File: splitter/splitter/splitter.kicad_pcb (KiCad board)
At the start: 2 copper layers, 50.8 x 89.4 mm, 35 parts, among them J1 JACKIN, J10 Conn_01x08, J11 Conn_01x08, J2 JACKSEND, J3 JACKRECV, J4 JACKOUT, J5 Jack-DC, J6 JACKSEND2, J7 RING_SEND, J8 JACKRECV2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

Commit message: more adjustments
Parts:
- moved U2 5.08 mm to (22.0, 21.8), turned to 90 degrees
- moved C3 5.01 mm to (23.4, 25.6), turned to -90 degrees
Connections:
- D1 pad 2: +9V -> /LED
- J10 pad 1: /DC_IN -> +9V
- J10 pad 2: +9V -> /LED
- J11 pad 1: /DC_IN_B -> /9V_B
- J11 pad 2: /9V_B -> /LED_B
- J5 pad 1: /DC_IN -> +9V
- SW2 pad 1: /9V_B -> /LED_B
- SW2 pad 2: /DC_IN_B -> /9V_B
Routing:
- net /DC_IN: track 99.7 -> 0.00 mm
- net /LED: track 0.00 -> 40.0 mm
- net /LED_B: track 0.00 -> 13.4 mm
- net /DC_IN_B: track 10.2 -> 0.00 mm
- net /SEND_WET: track 71.6 -> 63.4 mm, vias 1 -> 0
- net /HIGH: track 58.5 -> 65.0 mm, vias 1 -> 0
- net +9V: track 108.1 -> 113.3 mm
- net Net-(J3-PadR): track 41.7 -> 38.5 mm
- net /9V_B: track 13.5 -> 11.2 mm
- net /IN: track 78.3 -> 79.6 mm
- net Net-(C2-Pad1): track 22.8 -> 21.6 mm
- net /LOW: track 32.9 -> 33.7 mm
- net Net-(R9-Pad1): track 40.7 -> 41.4 mm
- net GND: vias 1 -> 0
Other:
- board text added: "JLCJLCJLCJLC"
- board text added: "REV.D TONE SPLITTER 2023-08-09"
- board text removed: "REV.C TONE SPLITTER 2023-08-31"

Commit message: rev D
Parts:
- removed J7: RING_SEND, Connector_PinSocket_2.54mm:PinSocket_1x02_P2.54mm_Vertical
- removed J9: RING_RECV, Connector_PinSocket_2.54mm:PinSocket_1x02_P2.54mm_Vertical
- removed the JP1 at (46.0, 62.9)
- added C10: .1u, kicad-official/Capacitor_THT.pretty:C_Rect_L7.0mm_W2.5mm_P5.00mm, F.Cu at (35.8, 55.9)
- added C5: .1u, kicad-official/Capacitor_THT.pretty:C_Rect_L7.0mm_W2.5mm_P5.00mm, F.Cu at (23.9, 55.9)
- added C6: .1u, kicad-official/Capacitor_THT.pretty:C_Rect_L7.0mm_W2.5mm_P5.00mm, F.Cu at (37.3, 37.6)
- added C7: .1u, kicad-official/Capacitor_THT.pretty:C_Rect_L7.0mm_W2.5mm_P5.00mm, F.Cu at (38.9, 19.3)
- added C8: .1u, kicad-official/Capacitor_THT.pretty:C_Rect_L7.0mm_W2.5mm_P5.00mm, F.Cu at (19.6, 36.4)
- added C9: .1u, kicad-official/Capacitor_THT.pretty:C_Rect_L7.0mm_W2.5mm_P5.00mm, F.Cu at (48.9, 33.8)
- added JP2: STEREO_MODE, kicad-official/Jumper.pretty:SolderJumper-3_P1.3mm_Open_RoundedPad1.0x1.5mm, F.Cu at (49.3, 56.9)
- added R11: 100K, kicad-official/Resistor_THT.pretty:R_Axial_DIN0207_L6.3mm_D2.5mm_P7.62mm_Horizontal, F.Cu at (50.0, 36.6)
- added R12: 100K, kicad-official/Resistor_THT.pretty:R_Axial_DIN0207_L6.3mm_D2.5mm_P7.62mm_Horizontal, F.Cu at (47.0, 36.6)
- C1, C2: footprint Capacitor_THT:C_Disc_D4.3mm_W1.9mm_P5.00mm -> kicad-official/Capacitor_THT.pretty:C_Disc_D4.3mm_W1.9mm_P5.00mm
- C3, C4: footprint Capacitor_THT:C_Rect_L7.0mm_W2.0mm_P5.00mm -> kicad-official/Capacitor_THT.pretty:CP_Radial_D5.0mm_P2.50mm
- D1: footprint LED_THT:LED_D3.0mm -> kicad-official/LED_THT.pretty:LED_D3.0mm
- J5: footprint Connector_PinSocket_2.54mm:PinSocket_1x02_P2.54mm_Vertical -> kicad-official/Connector_PinSocket_2.54mm.pretty:PinSocket_1x02_P2.54mm_Vertical
- JP1: renamed from JP2; footprint Jumper:SolderJumper-2_P1.3mm_Open_RoundedPad1.0x1.5mm -> kicad-official/Jumper.pretty:SolderJumper-2_P1.3mm_Open_RoundedPad1.0x1.5mm
- JP3: value JMP_RING_RECV -> STEREO_MODE_RETURN; footprint Jumper:SolderJumper-2_P1.3mm_Open_RoundedPad1.0x1.5mm -> kicad-official/Jumper.pretty:SolderJumper-3_P1.3mm_Open_RoundedPad1.0x1.5mm
- R1, R10, R2, R3, R4, R5, R6: footprint Resistor_THT:R_Axial_DIN0207_L6.3mm_D2.5mm_P7.62mm_Horizontal -> kicad-official/Resistor_THT.pretty:R_Axial_DIN0207_L6.3mm_D2.5mm_P7.62mm_Horizontal
- R7, R8: value 470K -> 100K; footprint Resistor_THT:R_Axial_DIN0207_L6.3mm_D2.5mm_P7.62mm_Horizontal -> kicad-official/Resistor_THT.pretty:R_Axial_DIN0207_L6.3mm_D2.5mm_P7.62mm_Horizontal
- R9: value 1M -> 1.2M; footprint Resistor_THT:R_Axial_DIN0207_L6.3mm_D2.5mm_P7.62mm_Horizontal -> kicad-official/Resistor_THT.pretty:R_Axial_DIN0207_L6.3mm_D2.5mm_P7.62mm_Horizontal
- RV1: footprint Potentiometer_THT:Potentiometer_Alpha_RD902F-40-00D_Dual_Vertical -> kicad-official/Potentiometer_THT.pretty:Potentiometer_Alpha_RD902F-40-00D_Dual_Vertical
- RV2: footprint Potentiometer_THT:Potentiometer_Alpha_RD901F-40-00D_Single_Vertical -> kicad-official/Potentiometer_THT.pretty:Potentiometer_Alpha_RD901F-40-00D_Single_Vertical
- U1: footprint Package_DIP:DIP-14_W7.62mm -> kicad-official/Package_DIP.pretty:DIP-14_W7.62mm_Socket
- U2: footprint Package_TO_SOT_THT:TO-92_Inline_Wide -> kicad-official/Package_TO_SOT_THT.pretty:TO-92_Inline_Wide
- moved JP3 8.31 mm to (10.4, 57.1), turned to 0 degrees
- moved R8 7.43 mm to (42.7, 29.8), turned to 0 degrees
- moved R10 6.04 mm to (43.9, 36.6)
- moved C4 3.47 mm to (36.1, 27.1), turned to -90 degrees
- moved R6 2.36 mm to (40.9, 36.6)
- moved C1 2.19 mm to (14.5, 43.7)
- moved C3 1.77 mm to (24.4, 27.1)
- moved C2 1.51 mm to (19.5, 40.0)
- moved R9 1.39 mm to (53.1, 36.6)
- moved R3 0.76 mm to (35.6, 19.6)
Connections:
- J1 pad S: GND -> GNDD
- J1 pad SN: GND -> GNDD
- J2 pad S: GND -> GNDD
- J2 pad SN: GND -> GNDD
- J2 pad T: /SEND_WET -> /SEND_1
- J3 pad R: Net-(J3-PadR) -> Net-(JP3-Pad2)
- J3 pad S: GND -> GNDD
- J3 pad SN: GND -> GNDD
- J3 pad T: /RECV_WET -> /RECV_1
- J3 pad TN: /SEND_WET -> /SEND_1
- J4 pad S: GND -> GNDD
- J4 pad SN: GND -> GNDD
- J6 pad S: GND -> GNDD
- J6 pad SN: GND -> GNDD
- J6 pad T: /SEND_DRY -> /SEND_2
- J8 pad S: GND -> GNDD
- J8 pad SN: GND -> GNDD
- J8 pad T: /RECV_DRY -> /RECV_2
- J8 pad TN: /SEND_DRY -> /SEND_2
- JP1 pad 1: /SEND_DRY -> /SEND_2
- JP1 pad 2: /RECV_DRY -> /RECV_2
- JP3 pad 1: Net-(J3-PadR) -> /RECVR
- JP3 pad 2: /RECVR -> Net-(JP3-Pad2)
- R4 pad 1: Net-(R4-Pad1) -> /IN
- R4 pad 2: /IN -> /HALF_IN
- R5 pad 2: Net-(R4-Pad1) -> /HALF_IN
- R7 pad 1: /RECV_WET -> Net-(R7-Pad1)
- R8 pad 2: /RECV_DRY -> Net-(R8-Pad2)
- R9 pad 2: /OUT -> Net-(R9-Pad2)
- RV2 pad 2: Net-(R9-Pad1) -> GND
- SW1 pad 2: /IN -> /HALF_IN
- SW1 pad 3: /SEND_WET -> Net-(SW1-Pad3)
- SW1 pad 6: GND -> /HALF_IN
- SW1 pad 7: /SEND_DRY -> Net-(SW1-Pad7)
- U1 pad 12: Net-(R4-Pad1) -> /HALF_IN
- U1 pad 5: /IN -> Net-(U1-Pad5)
- U1 pad 8: /OUT -> Net-(R9-Pad2)
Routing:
- net GND: track 0.00 -> 94.8 mm
- net /RECV_2: track 0.00 -> 94.8 mm
- net /SEND_2: track 0.00 -> 82.8 mm, vias 0 -> 1
- net /SEND_WET: track 63.4 -> 0.00 mm
- net /RECV_DRY: track 55.0 -> 0.00 mm
- net /HALF_IN: track 0.00 -> 54.9 mm
- net +9V: track 113.3 -> 62.6 mm
- net /IN: track 79.6 -> 30.8 mm
- net GNDD: track 49.1 -> 10.1 mm
- net Net-(J3-PadR): track 38.5 -> 0.00 mm
- net Net-(R7-Pad1): track 0.00 -> 37.4 mm
- net /SEND_DRY: track 35.7 -> 0.00 mm
- net /OUT: track 44.6 -> 12.1 mm
- net /SEND_1: track 0.00 -> 30.7 mm
- net Net-(R9-Pad2): track 0.00 -> 29.5 mm
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- added copper zone on B.Cu, net GNDD
- added copper zone on F.Cu, net GNDD
- removed copper zone on B.Cu, net GND
- removed copper zone on F.Cu, net GND
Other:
- board text added: "REV.D TONE SPLITTER 2023-08-30"
- board text removed: "REV.D TONE SPLITTER 2023-08-09"

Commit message: mechanicals and measurements
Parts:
- moved C1 1.00 mm to (14.5, 44.7)
- moved C10 1.00 mm to (35.8, 56.9)
- moved C2 1.00 mm to (19.5, 41.0)
- moved C3 1.00 mm to (24.4, 28.1)
- moved C4 1.00 mm to (36.1, 28.1)
- moved C5 1.00 mm to (23.9, 56.9)
- moved C6 1.00 mm to (37.3, 38.6)
- moved C7 1.00 mm to (38.9, 20.3)
- moved C8 1.00 mm to (19.6, 37.4)
- moved C9 1.00 mm to (48.9, 34.8)
- moved D1 1.00 mm to (31.5, 29.8)
- moved J1 1.00 mm to (40.0, 70.2)
- moved J10 1.00 mm to (26.2, 71.1)
- moved J11 1.00 mm to (26.2, 78.0)
- moved J2 1.00 mm to (40.0, 49.2)
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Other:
- board size 50.8 x 89.4 mm -> 50.8 x 92.4 mm
- board text added: "+"
- board text added: "REV.D TONE SPLITTER 2023-08-31"
- board text added: "knob1: 12.5,15.375 :: 7mm dia knob2: 47.5,15.375 :: 7mm dia switch: 30,(13.75+(21.75-13.75)/2)=>18.75 :: 7x2.5 => 10x4 LED: 30,29.75 :: 5 => 5.5mm dia stomp: 30,(90.85-6.85)=85 :: 11.8 => 12mm dia jacks: 10.95,27.2->19.1, 21mm spacing, 10mm dia 12.4 from surface to bottom of pcb. 11mm hole dia, 8mm from pcb to center 2mm case thickness -> 2+12.4+8 => 22.5mm from top jack1: 20,22.5 jack2: 41,22.5 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"
- board text added: "switch shift up 6.85mm"
- board text removed: "REV.D TONE SPLITTER 2023-08-30"
- board text removed: "switch shift up 6.858mm"

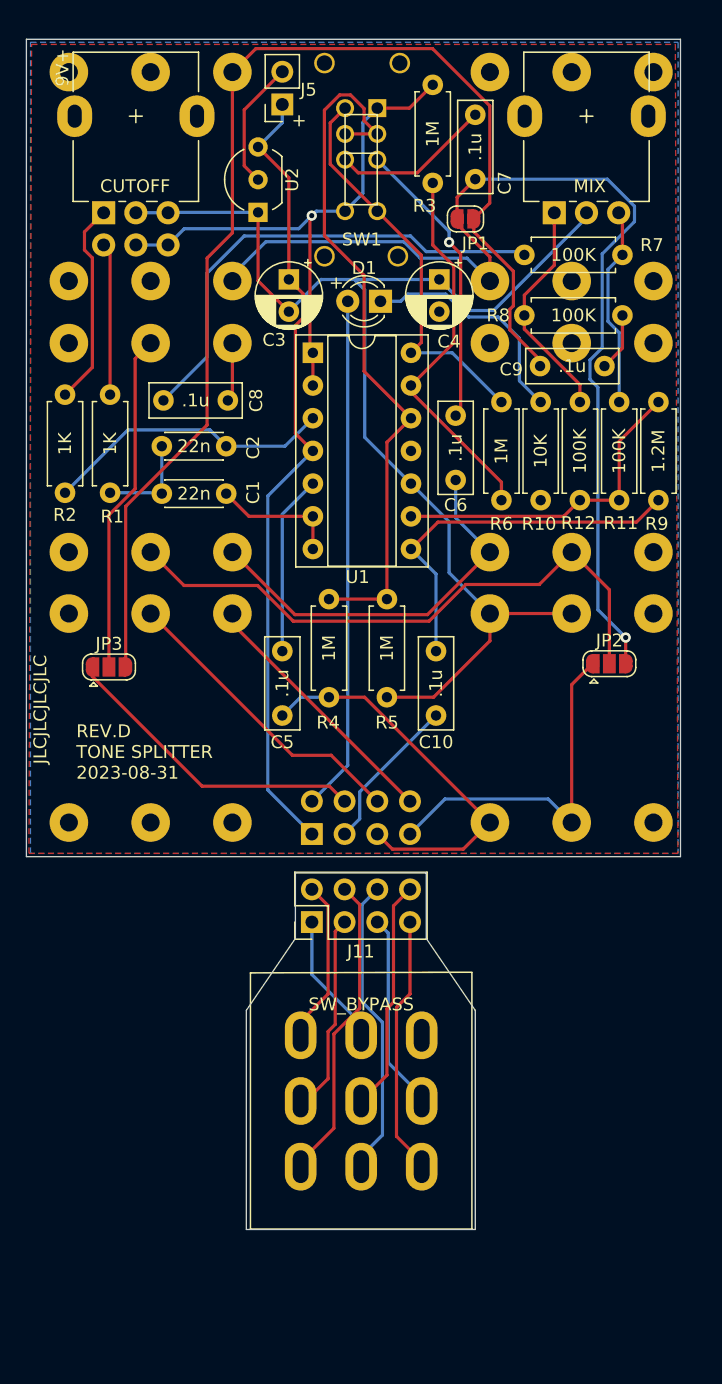
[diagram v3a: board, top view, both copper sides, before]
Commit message: fix some spacing, start on graphics
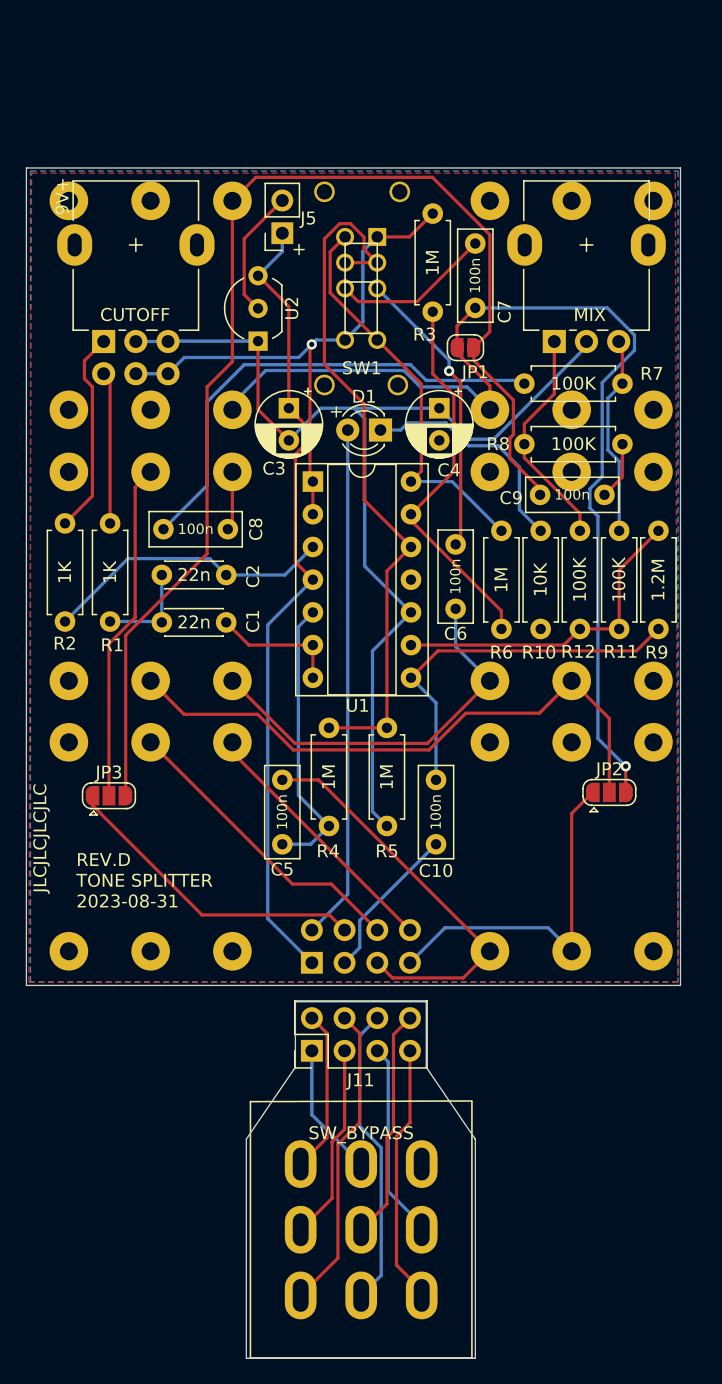
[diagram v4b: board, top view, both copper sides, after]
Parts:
- C10, C5, C6, C7, C8, C9: value .1u -> 100n
- moved C5 15.0 mm to (23.9, 71.9), turned to 90 degrees
- moved JP3 10.0 mm to (10.4, 68.2)
- moved RV1 10.0 mm to (10.0, 32.9)
- moved RV2 10.0 mm to (45.0, 32.9)
- moved C1 10.0 mm to (14.5, 54.7)
- moved C10 10.0 mm to (35.8, 66.9)
- moved C2 10.0 mm to (19.5, 51.0)
- moved C6 10.0 mm to (37.3, 48.6)
- moved C7 10.0 mm to (38.9, 30.3)
- moved C8 10.0 mm to (19.6, 47.4)
- moved C9 10.0 mm to (48.9, 44.8)
- moved D1 10.0 mm to (31.5, 39.8)
- moved J1 10.0 mm to (40.0, 80.2)
- moved J10 10.0 mm to (26.2, 81.1)
- moved J11 10.0 mm to (26.2, 88.0)
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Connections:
- C5 pad 1: Net-(U1-Pad5) -> Net-(C5-Pad1)
- J1 pad RN: GND -> GNDD
- J1 pad TN: GND -> GNDD
- R4 pad 1: /IN -> Net-(C5-Pad1)
- U1 pad 5: Net-(U1-Pad5) -> Net-(C5-Pad1)
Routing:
- net Net-(C5-Pad1): track 0.00 -> 22.3 mm
- net Net-(U1-Pad5): track 14.0 -> 0.00 mm
- net GND: track 94.8 -> 82.2 mm
- net /RECVR_B: track 23.0 -> 23.9 mm
- net /IN: track 30.8 -> 31.7 mm
- net /9V_B: track 9.49 -> 10.4 mm
- net /OUTR_B: track 22.6 -> 23.4 mm
- net /LED_B: track 13.4 -> 12.7 mm

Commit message: rework graphics and finalize case
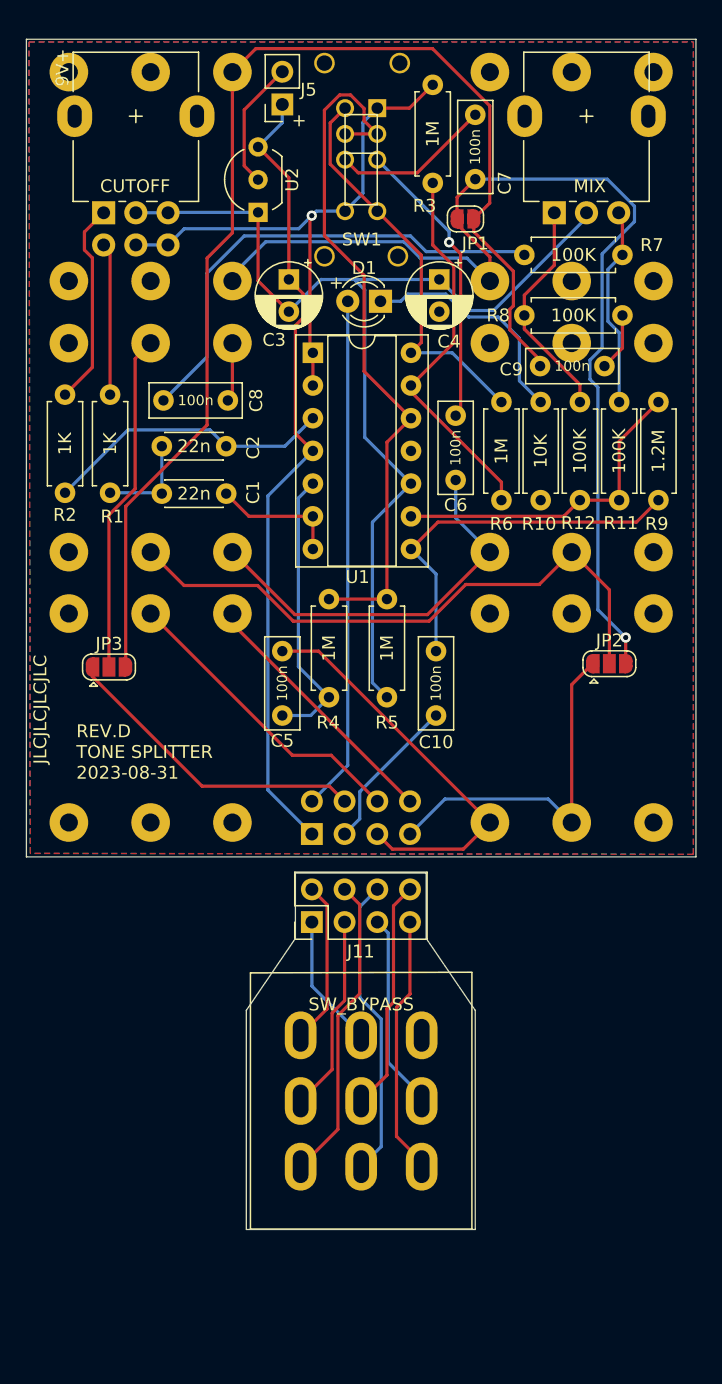
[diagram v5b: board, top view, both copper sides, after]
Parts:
- moved JP3 10.0 mm to (10.4, 58.1)
- moved RV1 10.0 mm to (10.0, 22.9)
- moved RV2 10.0 mm to (45.0, 22.9)
- moved C1 10.0 mm to (14.5, 44.7)
- moved C10 10.0 mm to (35.8, 56.9)
- moved C2 10.0 mm to (19.5, 41.0)
- moved C5 10.0 mm to (23.9, 61.9)
- moved C6 10.0 mm to (37.3, 38.6)
- moved C7 10.0 mm to (38.9, 20.3)
- moved C8 10.0 mm to (19.6, 37.4)
- moved C9 10.0 mm to (48.9, 34.8)
- moved D1 10.0 mm to (31.5, 29.8)
- moved J1 10.0 mm to (40.0, 70.2)
- moved J10 10.0 mm to (26.2, 71.1)
- moved J11 10.0 mm to (26.2, 78.0)
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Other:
- board size 50.8 x 92.4 mm -> 52 x 92.4 mm
- board text added: "knob1: 12.5,14.375 :: 7mm dia knob2: 47.5,14.375 :: 7mm dia switch: 30,(13.75+(21.75-13.75)/2)=>17.75 :: 7x2.5 => 10x4 LED: 30,28.75 :: 5 => 5.5mm dia stomp: 30,(90.85-6.85)=84 :: 11.8 => 12mm dia jacks: 10.95,27.2->19.1, 21mm spacing, 10mm dia 12.4 from surface to bottom of pcb. 11mm hole dia, 8mm from pcb to center 2mm case thickness -> 2+12.4+8 => 22.5mm from top jack1: 19,22.5 jack2: 40,22.5 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"
- board text removed: "knob1: 12.5,15.375 :: 7mm dia knob2: 47.5,15.375 :: 7mm dia switch: 30,(13.75+(21.75-13.75)/2)=>18.75 :: 7x2.5 => 10x4 LED: 30,29.75 :: 5 => 5.5mm dia stomp: 30,(90.85-6.85)=85 :: 11.8 => 12mm dia jacks: 10.95,27.2->19.1, 21mm spacing, 10mm dia 12.4 from surface to bottom of pcb. 11mm hole dia, 8mm from pcb to center 2mm case thickness -> 2+12.4+8 => 22.5mm from top jack1: 20,22.5 jack2: 41,22.5 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"
